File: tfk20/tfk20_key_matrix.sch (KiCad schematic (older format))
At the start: 40 parts

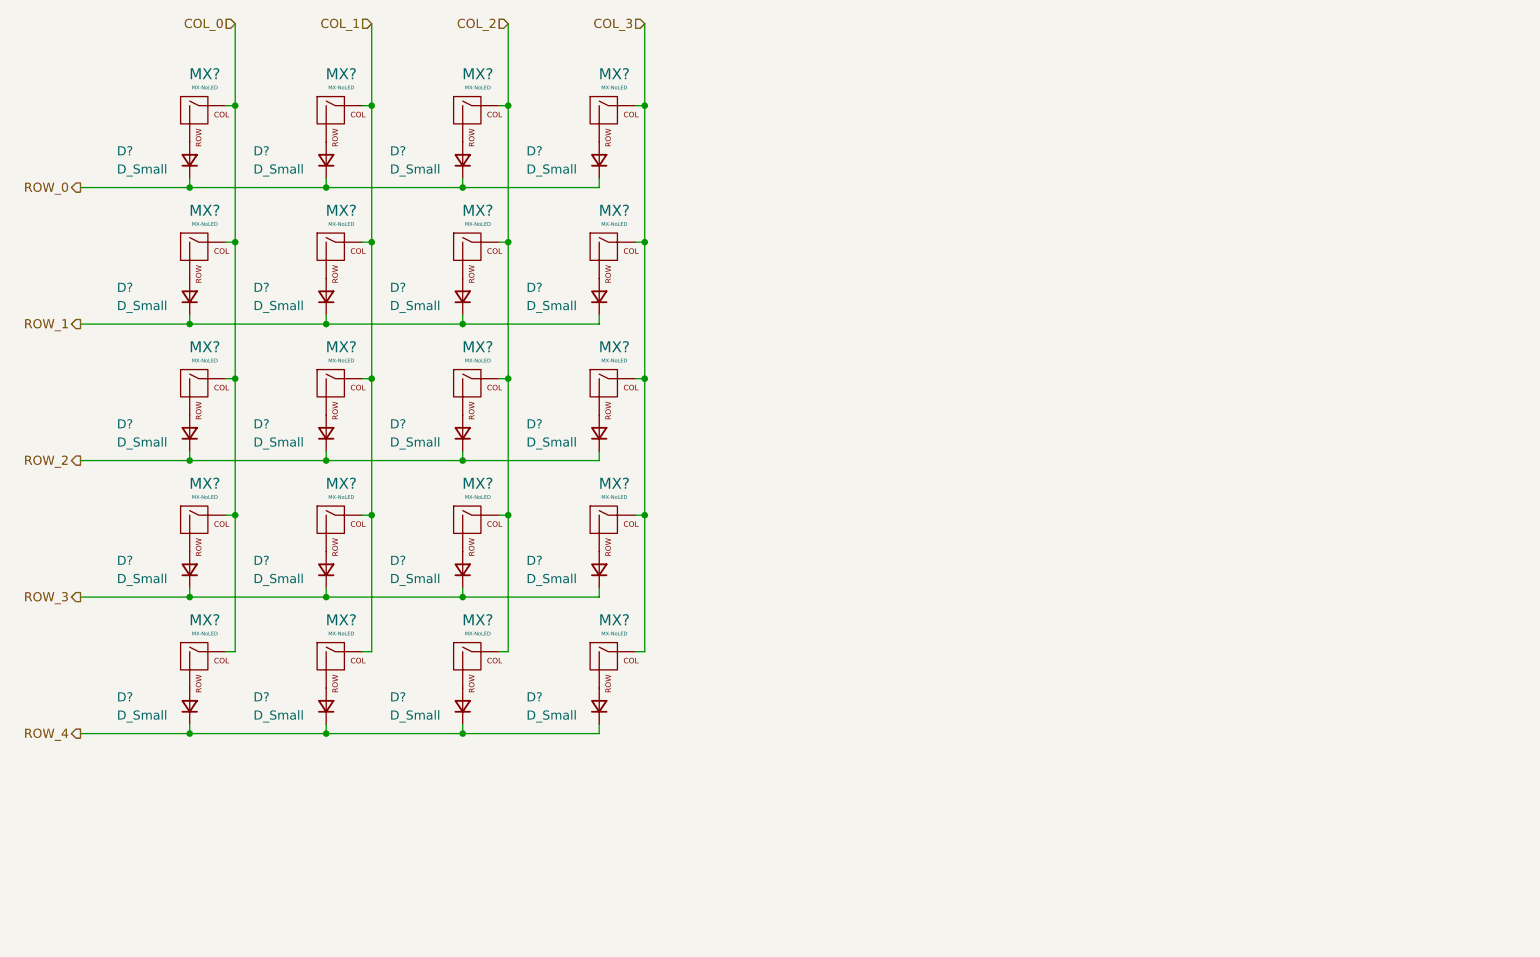
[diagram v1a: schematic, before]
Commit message: Change MCU, add another row, add reset button
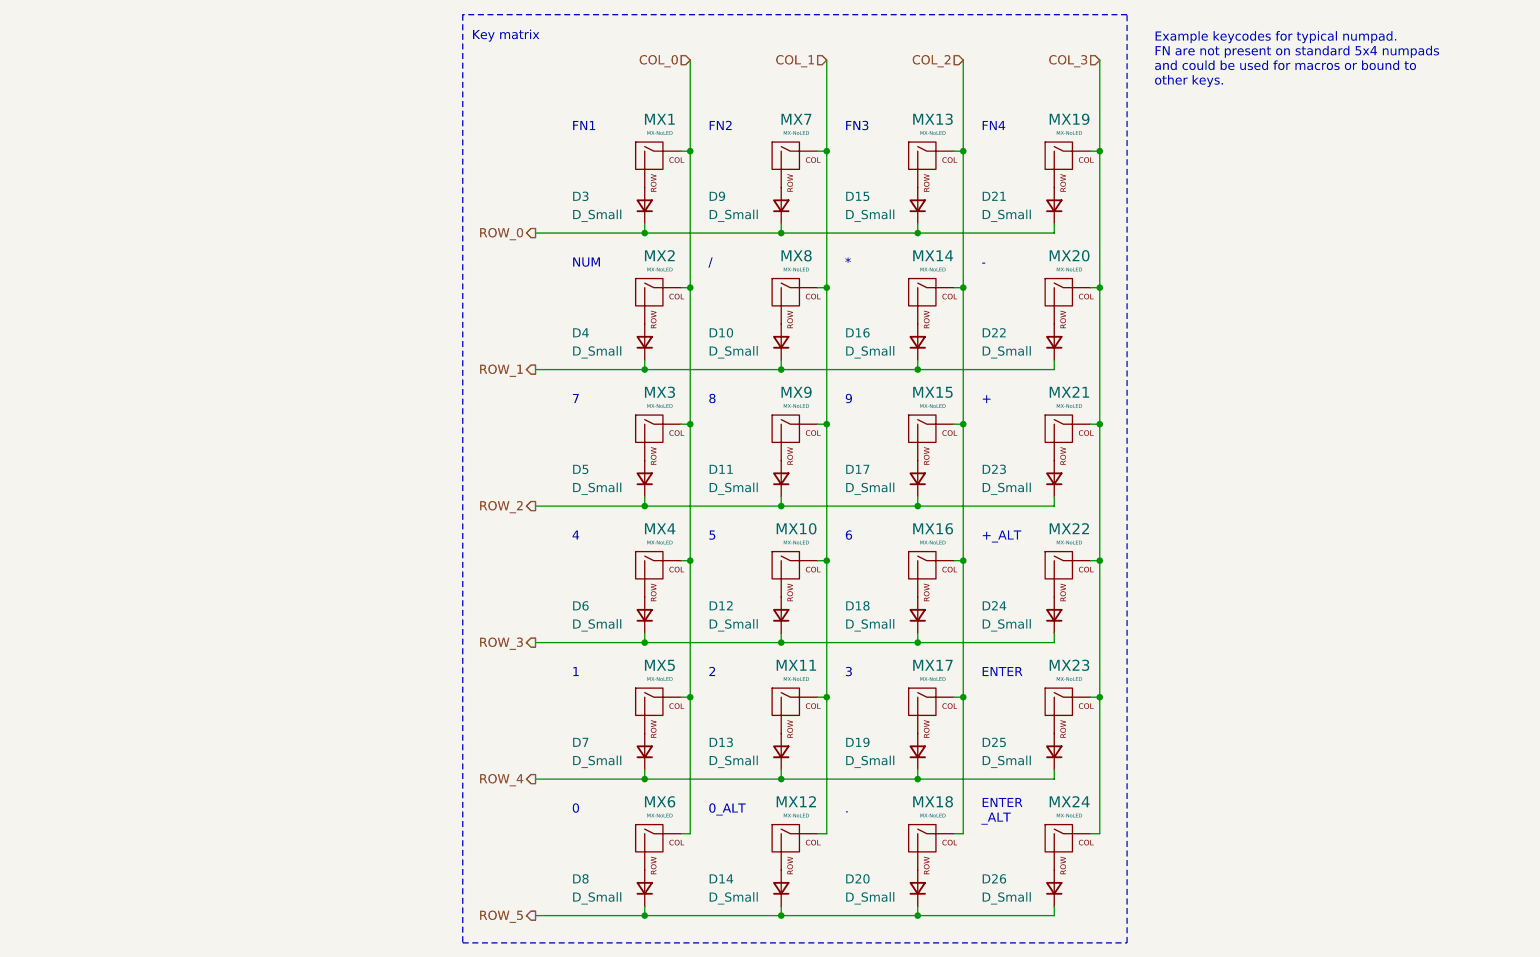
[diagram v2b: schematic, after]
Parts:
- added D15, D21, D3, D9: D_Small, symbol Device:D_Small
- added MX1, MX13, MX19, MX7: MX-NoLED, symbol MX_Alps_Hybrid:MX-NoLED
- gave numbers to parts that had none: 40
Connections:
- net COL_0: now also MX1.1 (COL)
- net COL_1: now also MX7.1 (COL)
- net COL_2: now also MX13.1 (COL)
- net COL_3: now also MX19.1 (COL)
- net ROW_0: now also D15.1 (K), D21.1 (K), D3.1 (K), D9.1 (K); no longer D10.1 (K), D16.1 (K), D22.1 (K), D4.1 (K)
- net ROW_1: now also D10.1 (K), D16.1 (K), D22.1 (K), D4.1 (K); no longer D11.1 (K), D17.1 (K), D23.1 (K), D5.1 (K)
- net ROW_2: now also D11.1 (K), D17.1 (K), D23.1 (K), D5.1 (K); no longer D12.1 (K), D18.1 (K), D24.1 (K), D6.1 (K)
- net ROW_3: now also D12.1 (K), D18.1 (K), D24.1 (K), D6.1 (K); no longer D13.1 (K), D19.1 (K), D25.1 (K), D7.1 (K)
- net ROW_4: now also D13.1 (K), D19.1 (K), D25.1 (K), D7.1 (K); no longer D14.1 (K), D20.1 (K), D26.1 (K), D8.1 (K)
- new net: D3.2 (A), MX1.2 (ROW)
- new net: D9.2 (A), MX7.2 (ROW)
- new net: D15.2 (A), MX13.2 (ROW)
- new net: D21.2 (A), MX19.2 (ROW)
- new net ROW_5: D14.1 (K), D20.1 (K), D26.1 (K), D8.1 (K)
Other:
- note added: "*"
- note added: "+"
- note added: "+_ALT"
- note added: "-"
- note added: "."
- note added: "/"
- note added: "0"
- note added: "0_ALT"
- note added: "1"
- note added: "2"
- note added: "3"
- note added: "4"
- note added: "5"
- note added: "6"
- note added: "7"
- note added: "8"
- note added: "9"
- note added: "ENTER"
- note added: "ENTER\n_ALT"
- note added: "Example keycodes for typical numpad.\nFN are not present on standard 5x4 numpads\nand could be used for macros or bound to\nother keys."
- note added: "FN1"
- note added: "FN2"
- note added: "FN3"
- note added: "FN4"
- note added: "Key matrix"
- note added: "NUM\n"
- moved on the sheet: D10, D11, D12, D13, D14, D16, D17, D18, D19, D20, D22, D23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

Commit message: Add STL11N3LLH6 footprint
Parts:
- renumbered D3 to D201, D4 to D202, D5 to D203, D6 to D204, D7 to D205, D8 to D206, D9 to D207, D10 to D208, D11 to D209, D12 to D210, D13 to D211, D14 to D212, D15 to D213, D16 to D214, D17 to D215, D18 to D216, D19 to D217, D20 to D218, D21 to D219, D22 to D220, D23 to D221, D24 to D222, D25 to D223, D26 to D224, MX1 to MX201, MX2 to MX202, MX3 to MX203, MX4 to MX204, MX5 to MX205, MX6 to MX206, MX7 to MX207, MX8 to MX208, MX9 to MX209, MX10 to MX210, MX11 to MX211, MX12 to MX212, MX13 to MX213, MX14 to MX214, MX15 to MX215, MX16 to MX216, MX17 to MX217, MX18 to MX218, MX19 to MX219, MX20 to MX220, MX21 to MX221, MX22 to MX222, MX23 to MX223, MX24 to MX224
